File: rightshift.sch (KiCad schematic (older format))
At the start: 15 parts

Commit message: Some minor edits
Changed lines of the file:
@@
 	5825 2425 6125 2425
 Wire Wire Line
-	6125 3625 6125 2425
+	6125 2425 6125 3625
 Wire Wire Line
 	6125 3000 5825 3000
@@
 	4775 3575 4775 3625
 Wire Wire Line
-	4750 3625 6125 3625
+	6125 3625 4750 3625
 Wire Wire Line
 	5825 3625 5825 3575

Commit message: Fix all key annotations
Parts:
- renumbered RS1 to K_RS1, RS2 to K_RS2, RS3 to K_RS3, RS4 to K_RS4, RS5 to K_RS5, RS6 to K_RS6, RS7 to K_RS7, RS8 to K_RS8, RS9 to K_RS9
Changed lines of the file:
@@
 $EndDescr
 $Comp
-L MX-1U RS1
+L MX-1U K_RS1
 U 1 1 591D166F
 P 4800 2250
-F 0 "RS1" H 4800 2375 60  0000 C CNN
+F 0 "K_RS1" H 4800 2375 60  0000 C CNN
 F 1 "MX-1U" H 4800 2300 20  0000 C CNN
 F 2 "" H 4775 2225 60  0001 C CNN
@@
 $EndComp
 $Comp
-L MX-1.25U RS2
+L MX-1.25U K_RS2
 U 1 1 591D16FE
 P 4800 2825
-F 0 "RS2" H 4800 2950 60  0000 C CNN
+F 0 "K_RS2" H 4800 2950 60  0000 C CNN
 F 1 "MX-1.25U" H 4800 2875 20  0000 C CNN
 F 2 "" H 4775 2800 60  0001 C CNN
@@
 $EndComp
 $Comp
-L MX-1.25U RS3
+L MX-1.25U K_RS3
 U 1 1 591D173D
 P 4800 3400
-F 0 "RS3" H 4800 3525 60  0000 C CNN
+F 0 "K_RS3" H 4800 3525 60  0000 C CNN
 F 1 "MX-1.25U" H 4800 3450 20  0000 C CNN
 F 2 "" H 4775 3375 60  0001 C CNN
@@
 $EndComp
 $Comp
-L MX-1U RS4
+L MX-1U K_RS4
 U 1 1 591D189D
 P 5325 2250
-F 0 "RS4" H 5325 2375 60  0000 C CNN
+F 0 "K_RS4" H 5325 2375 60  0000 C CNN
 F 1 "MX-1U" H 5325 2300 20  0000 C CNN
 F 2 "" H 5300 2225 60  0001 C CNN
@@
 $EndComp
 $Comp
-L MX-1.75U RS5
+L MX-1.75U K_RS5
 U 1 1 591D19CC
 P 5325 2825
-F 0 "RS5" H 5325 2950 60  0000 C CNN
+F 0 "K_RS5" H 5325 2950 60  0000 C CNN
 F 1 "MX-1.75U" H 5325 2875 20  0000 C CNN
 F 2 "" H 5300 2800 60  0001 C CNN
@@
 $EndComp
 $Comp
-L MX-2.75U RS6
+L MX-2.75U K_RS6
 U 1 1 591D1A90
 P 5325 3400
-F 0 "RS6" H 5325 3525 60  0000 C CNN
+F 0 "K_RS6" H 5325 3525 60  0000 C CNN
 F 1 "MX-2.75U" H 5325 3450 20  0000 C CNN
 F 2 "" H 5300 3375 60  0001 C CNN
@@
 $EndComp
 $Comp
-L MX-1U RS7
+L MX-1U K_RS7
 U 1 1 591D21A1
 P 5850 2250
-F 0 "RS7" H 5850 2375 60  0000 C CNN
+F 0 "K_RS7" H 5850 2375 60  0000 C CNN
 F 1 "MX-1U" H 5850 2300 20  0000 C CNN
 F 2 "" H 5825 2225 60  0001 C CNN
@@
 $EndComp
 $Comp
-L MX-1.75U RS8
+L MX-1.75U K_RS8
 U 1 1 591D25C2
 P 5850 2825
-F 0 "RS8" H 5850 2950 60  0000 C CNN
+F 0 "K_RS8" H 5850 2950 60  0000 C CNN
 F 1 "MX-1.75U" H 5850 2875 20  0000 C CNN
 F 2 "" H 5825 2800 60  0001 C CNN
@@
 $EndComp
 $Comp
-L MX-2U RS9
+L MX-2U K_RS9
 U 1 1 591D28C1
 P 5850 3400
-F 0 "RS9" H 5850 3525 60  0000 C CNN
+F 0 "K_RS9" H 5850 3525 60  0000 C CNN
 F 1 "MX-2U" H 5850 3450 20  0000 C CNN
 F 2 "" H 5825 3375 60  0001 C CNN

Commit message: Fix left shift, associate MX footprints
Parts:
- K_RS1, K_RS4, K_RS7: footprint (none) -> MX_Alps_Hybrid:MX-1U
- K_RS2, K_RS3: footprint (none) -> MX_Alps_Hybrid:MX-1.25U
- K_RS5, K_RS8: footprint (none) -> MX_Alps_Hybrid:MX-1.75U
- K_RS6: footprint (none) -> MX_Alps_Hybrid:MX-2.75U
- K_RS9: footprint (none) -> MX_Alps_Hybrid:MX-2U
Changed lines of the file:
@@
 F 0 "K_RS1" H 4800 2375 60  0000 C CNN
 F 1 "MX-1U" H 4800 2300 20  0000 C CNN
-F 2 "" H 4775 2225 60  0001 C CNN
+F 2 "MX_Alps_Hybrid:MX-1U" H 4775 2225 60  0001 C CNN
 F 3 "" H 4775 2225 60  0001 C CNN
 	1    4800 2250
@@
 F 0 "K_RS2" H 4800 2950 60  0000 C CNN
 F 1 "MX-1.25U" H 4800 2875 20  0000 C CNN
-F 2 "" H 4775 2800 60  0001 C CNN
+F 2 "MX_Alps_Hybrid:MX-1.25U" H 4775 2800 60  0001 C CNN
 F 3 "" H 4775 2800 60  0001 C CNN
 	1    4800 2825
@@
 F 0 "K_RS3" H 4800 3525 60  0000 C CNN
 F 1 "MX-1.25U" H 4800 3450 20  0000 C CNN
-F 2 "" H 4775 3375 60  0001 C CNN
+F 2 "MX_Alps_Hybrid:MX-1.25U" H 4775 3375 60  0001 C CNN
 F 3 "" H 4775 3375 60  0001 C CNN
 	1    4800 3400
@@
 F 0 "K_RS4" H 5325 2375 60  0000 C CNN
 F 1 "MX-1U" H 5325 2300 20  0000 C CNN
-F 2 "" H 5300 2225 60  0001 C CNN
+F 2 "MX_Alps_Hybrid:MX-1U" H 5300 2225 60  0001 C CNN
 F 3 "" H 5300 2225 60  0001 C CNN
 	1    5325 2250
@@
 F 0 "K_RS5" H 5325 2950 60  0000 C CNN
 F 1 "MX-1.75U" H 5325 2875 20  0000 C CNN
-F 2 "" H 5300 2800 60  0001 C CNN
+F 2 "MX_Alps_Hybrid:MX-1.75U" H 5300 2800 60  0001 C CNN
 F 3 "" H 5300 2800 60  0001 C CNN
 	1    5325 2825
@@
 F 0 "K_RS6" H 5325 3525 60  0000 C CNN
 F 1 "MX-2.75U" H 5325 3450 20  0000 C CNN
-F 2 "" H 5300 3375 60  0001 C CNN
+F 2 "MX_Alps_Hybrid:MX-2.75U" H 5300 3375 60  0001 C CNN
 F 3 "" H 5300 3375 60  0001 C CNN
 	1    5325 3400
@@
 F 0 "K_RS7" H 5850 2375 60  0000 C CNN
 F 1 "MX-1U" H 5850 2300 20  0000 C CNN
-F 2 "" H 5825 2225 60  0001 C CNN
+F 2 "MX_Alps_Hybrid:MX-1U" H 5825 2225 60  0001 C CNN
 F 3 "" H 5825 2225 60  0001 C CNN
 	1    5850 2250
@@
 F 0 "K_RS8" H 5850 2950 60  0000 C CNN
 F 1 "MX-1.75U" H 5850 2875 20  0000 C CNN
-F 2 "" H 5825 2800 60  0001 C CNN
+F 2 "MX_Alps_Hybrid:MX-1.75U" H 5825 2800 60  0001 C CNN
 F 3 "" H 5825 2800 60  0001 C CNN
 	1    5850 2825
@@
 F 0 "K_RS9" H 5850 3525 60  0000 C CNN
 F 1 "MX-2U" H 5850 3450 20  0000 C CNN
-F 2 "" H 5825 3375 60  0001 C CNN
+F 2 "MX_Alps_Hybrid:MX-2U" H 5825 3375 60  0001 C CNN
 F 3 "" H 5825 3375 60  0001 C CNN
 	1    5850 3400
@@
 F 0 "DRS1" H 5050 1950 50  0000 C CNN
 F 1 "1N4148WS" H 5050 1750 50  0000 C CNN
-F 2 "" H 5050 1850 50  0000 C CNN
+F 2 "" H 5050 1850 50  0001 C CNN
 F 3 "" H 5050 1850 50  0000 C CNN
 	1    5050 1850
@@
 F 0 "DRS2" H 5575 1950 50  0000 C CNN
 F 1 "1N4148WS" H 5575 1750 50  0000 C CNN
-F 2 "" H 5575 1850 50  0000 C CNN
+F 2 "" H 5575 1850 50  0001 C CNN
 F 3 "" H 5575 1850 50  0000 C CNN
 	1    5575 1850
@@
 F 0 "DRS3" H 6100 1950 50  0000 C CNN
 F 1 "1N4148WS" H 6100 1750 50  0000 C CNN
-F 2 "" H 6100 1850 50  0000 C CNN
+F 2 "" H 6100 1850 50  0001 C CNN
 F 3 "" H 6100 1850 50  0000 C CNN
 	1    6100 1850
@@
 F 0 "RRS1" V 5180 3950 50  0000 C CNN
 F 1 "2.2k" V 5100 3950 50  0000 C CNN
-F 2 "" V 5030 3950 50  0000 C CNN
+F 2 "" V 5030 3950 50  0001 C CNN
 F 3 "" H 5100 3950 50  0000 C CNN
 	1    5100 3950
@@
 F 0 "RRS2" V 5705 3950 50  0000 C CNN
 F 1 "2.2k" V 5625 3950 50  0000 C CNN
-F 2 "" V 5555 3950 50  0000 C CNN
+F 2 "" V 5555 3950 50  0001 C CNN
 F 3 "" H 5625 3950 50  0000 C CNN
 	1    5625 3950
@@
 F 0 "RRS3" V 6230 3950 50  0000 C CNN
 F 1 "2.2k" V 6150 3950 50  0000 C CNN
-F 2 "" V 6080 3950 50  0000 C CNN
+F 2 "" V 6080 3950 50  0001 C CNN
 F 3 "" H 6150 3950 50  0000 C CNN
 	1    6150 3950

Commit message: Halfway fix RS2
Failed to load cvpcb
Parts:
- K_RS2: value MX-1.25U -> MX-1.75U; footprint MX_Alps_Hybrid:MX-1.25U -> MX_Alps_Hybrid:MX-1.75U
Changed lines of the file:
@@
 P 4800 2825
 F 0 "K_RS2" H 4800 2950 60  0000 C CNN
-F 1 "MX-1.25U" H 4800 2875 20  0000 C CNN
-F 2 "MX_Alps_Hybrid:MX-1.25U" H 4775 2800 60  0001 C CNN
+F 1 "MX-1.75U" H 4800 2875 20  0000 C CNN
+F 2 "MX_Alps_Hybrid:MX-1.75U" H 4775 2800 60  0001 C CNN
 F 3 "" H 4775 2800 60  0001 C CNN
 	1    4800 2825

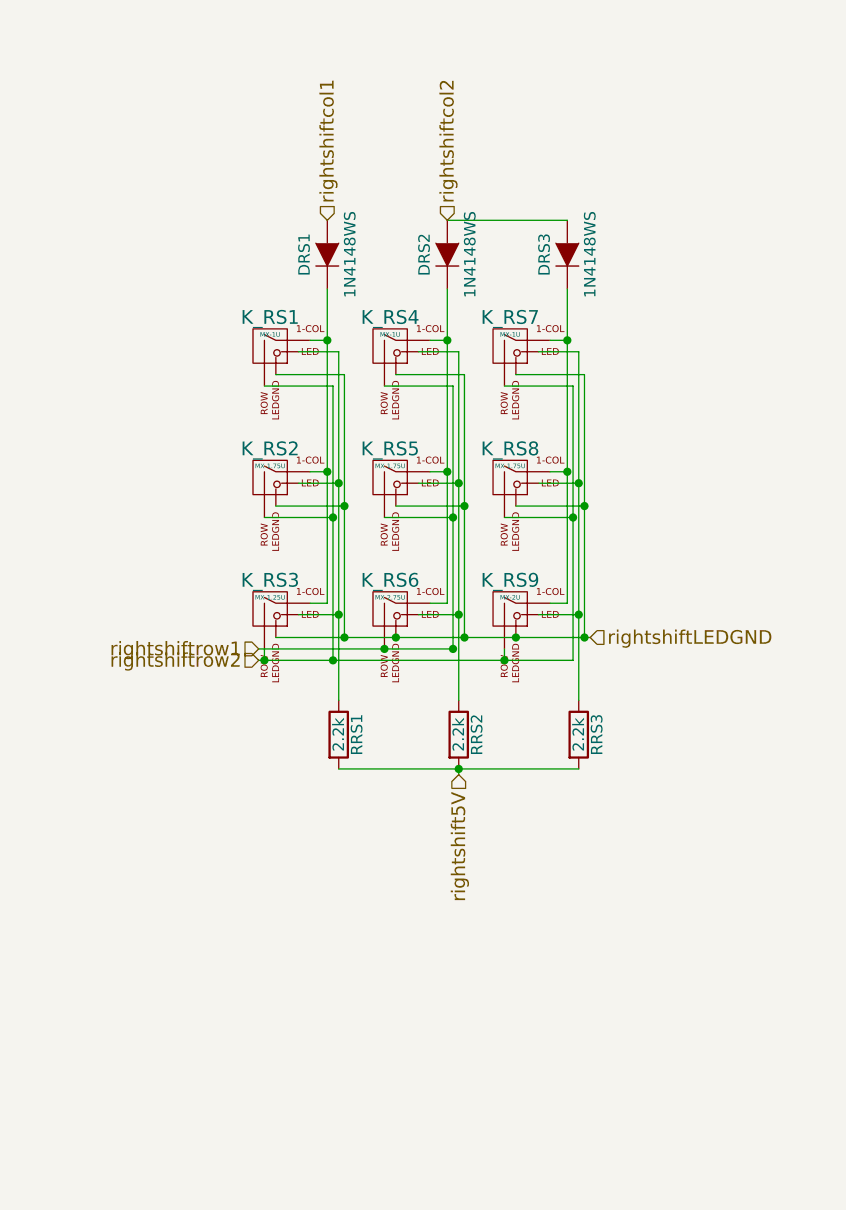
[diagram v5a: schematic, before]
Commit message: Fix RShift Diode Location
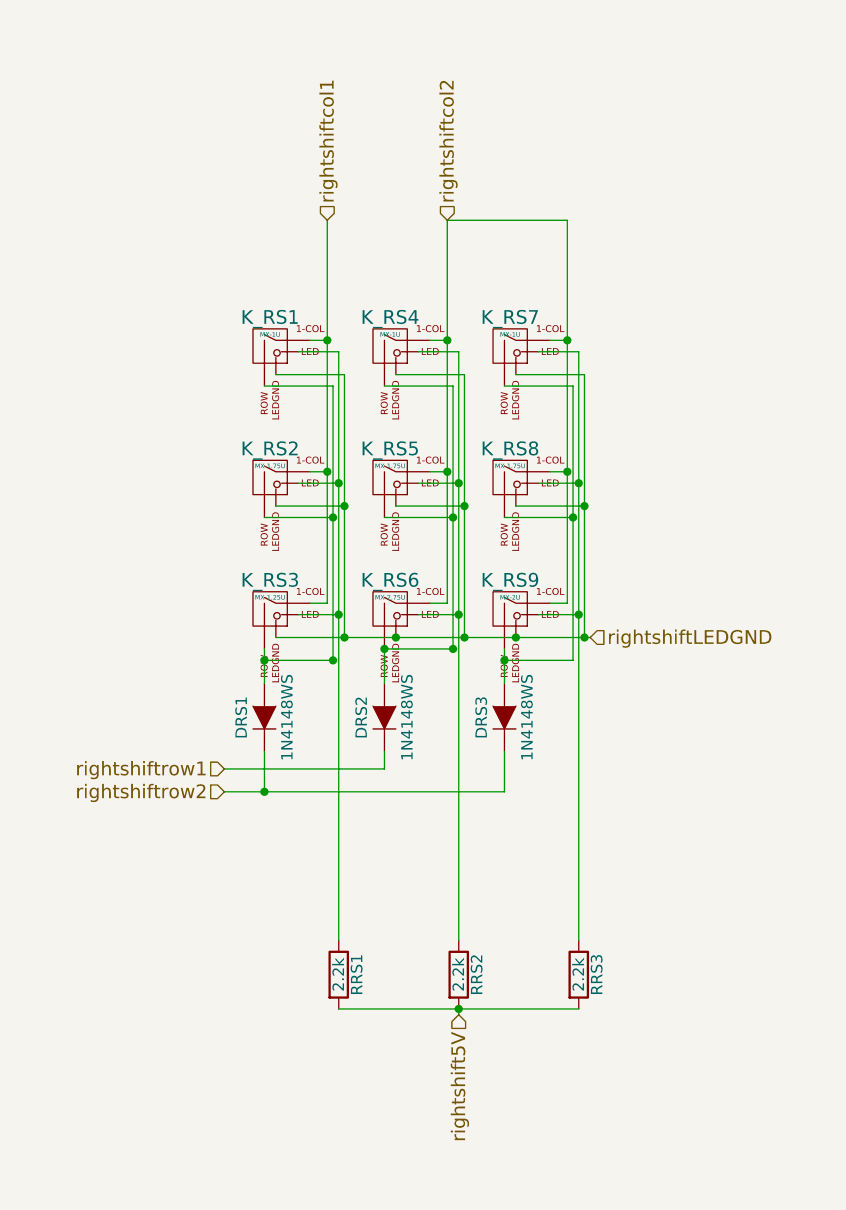
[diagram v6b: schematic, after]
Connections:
- net rightshiftcol1: now also K_RS1.1 (COL), K_RS2.1 (COL), K_RS3.1 (COL); no longer DRS1.2 (A)
- net rightshiftcol2: now also K_RS4.1 (COL), K_RS5.1 (COL), K_RS6.1 (COL), K_RS7.1 (COL), K_RS8.1 (COL), K_RS9.1 (COL); no longer DRS2.2 (A), DRS3.2 (A)
- net rightshiftrow1: now also DRS2.1 (K); no longer K_RS4.2 (ROW), K_RS5.2 (ROW), K_RS6.2 (ROW)
- net rightshiftrow2: now also DRS1.1 (K), DRS3.1 (K); no longer K_RS1.2 (ROW), K_RS2.2 (ROW), K_RS3.2 (ROW), K_RS7.2 (ROW), K_RS8.2 (ROW), K_RS9.2 (ROW)
- new net: DRS1.2 (A), K_RS1.2 (ROW), K_RS2.2 (ROW), K_RS3.2 (ROW)
- new net: DRS2.2 (A), K_RS4.2 (ROW), K_RS5.2 (ROW), K_RS6.2 (ROW)
- new net: DRS3.2 (A), K_RS7.2 (ROW), K_RS8.2 (ROW), K_RS9.2 (ROW)
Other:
- moved on the sheet: DRS1, DRS2, DRS3, RRS1, RRS2, RRS3
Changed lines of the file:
@@
 	4975 2225 5050 2225
 Wire Wire Line
-	5050 2000 5050 3375
+	5050 1700 5050 3375
 Wire Wire Line
 	5050 2800 4975 2800
@@
 	5500 2225 5575 2225
 Wire Wire Line
-	5575 2000 5575 3375
+	5575 1700 5575 3375
 Wire Wire Line
 	5575 2800 5500 2800
@@
 	6025 2225 6100 2225
 Wire Wire Line
-	6100 2000 6100 3375
+	6100 1700 6100 3375
 Wire Wire Line
 	6100 2800 6025 2800
@@
 	5075 3000 4775 3000
 Wire Wire Line
-	5600 3575 4750 3575
+	5600 3575 5300 3575
 Connection ~ 5075 3000
 Wire Wire Line
@@
 	4925 2275 5100 2275
 Wire Wire Line
-	5100 2275 5100 3800
+	5100 2275 5100 4850
 Wire Wire Line
 	5100 2850 4925 2850
@@
 	5450 2275 5625 2275
 Wire Wire Line
-	5625 2275 5625 3800
+	5625 2275 5625 4850
 Wire Wire Line
 	5625 2850 5450 2850
@@
 	5975 2275 6150 2275
 Wire Wire Line
-	6150 2275 6150 3800
+	6150 2275 6150 4850
 Wire Wire Line
 	6150 2850 5975 2850
@@
 L D DRS1
 U 1 1 591D56E3
-P 5050 1850
-F 0 "DRS1" H 5050 1950 50  0000 C CNN
-F 1 "1N4148WS" H 5050 1750 50  0000 C CNN
-F 2 "" H 5050 1850 50  0001 C CNN
-F 3 "" H 5050 1850 50  0000 C CNN
-	1    5050 1850
+P 4775 3875
+F 0 "DRS1" H 4775 3975 50  0000 C CNN
+F 1 "1N4148WS" H 4775 3775 50  0000 C CNN
+F 2 "" H 4775 3875 50  0001 C CNN
+F 3 "" H 4775 3875 50  0000 C CNN
+	1    4775 3875
 	0    -1   -1   0
 $EndComp
@@
 L D DRS2
 U 1 1 591D57BD
-P 5575 1850
-F 0 "DRS2" H 5575 1950 50  0000 C CNN
-F 1 "1N4148WS" H 5575 1750 50  0000 C CNN
-F 2 "" H 5575 1850 50  0001 C CNN
-F 3 "" H 5575 1850 50  0000 C CNN
-	1    5575 1850
+P 5300 3875
+F 0 "DRS2" H 5300 3975 50  0000 C CNN
+F 1 "1N4148WS" H 5300 3775 50  0000 C CNN
+F 2 "" H 5300 3875 50  0001 C CNN
+F 3 "" H 5300 3875 50  0000 C CNN
+	1    5300 3875
 	0    -1   -1   0
 $EndComp
@@
 L D DRS3
 U 1 1 591D583A
-P 6100 1850
-F 0 "DRS3" H 6100 1950 50  0000 C CNN
-F 1 "1N4148WS" H 6100 1750 50  0000 C CNN
-F 2 "" H 6100 1850 50  0001 C CNN
-F 3 "" H 6100 1850 50  0000 C CNN
-	1    6100 1850
+P 5825 3875
+F 0 "DRS3" H 5825 3975 50  0000 C CNN
+F 1 "1N4148WS" H 5825 3775 50  0000 C CNN
+F 2 "" H 5825 3875 50  0001 C CNN
+F 3 "" H 5825 3875 50  0000 C CNN
+	1    5825 3875
 	0    -1   -1   0
 $EndComp
@@
 Connection ~ 6100 2225
 Connection ~ 5575 2225
-Text HLabel 4750 3575 0    60   Input ~ 0
+Text HLabel 4600 4100 0    60   Input ~ 0
 rightshiftrow1
 $Comp
 L R RRS1
 U 1 1 591D6B12
-P 5100 3950
-F 0 "RRS1" V 5180 3950 50  0000 C CNN
-F 1 "2.2k" V 5100 3950 50  0000 C CNN
-F 2 "" V 5030 3950 50  0001 C CNN
-F 3 "" H 5100 3950 50  0000 C CNN
-	1    5100 3950
+P 5100 5000
+F 0 "RRS1" V 5180 5000 50  0000 C CNN
+F 1 "2.2k" V 5100 5000 50  0000 C CNN
+F 2 "" V 5030 5000 50  0001 C CNN
+F 3 "" H 5100 5000 50  0000 C CNN
+	1    5100 5000
 	1    0    0    -1
 $EndComp
@@
 L R RRS2
 U 1 1 591D713D
-P 5625 3950
-F 0 "RRS2" V 5705 3950 50  0000 C CNN
-F 1 "2.2k" V 5625 3950 50  0000 C CNN
-F 2 "" V 5555 3950 50  0001 C CNN
-F 3 "" H 5625 3950 50  0000 C CNN
-	1    5625 3950
+P 5625 5000
+F 0 "RRS2" V 5705 5000 50  0000 C CNN
+F 1 "2.2k" V 5625 5000 50  0000 C CNN
+F 2 "" V 5555 5000 50  0001 C CNN
+F 3 "" H 5625 5000 50  0000 C CNN
+	1    5625 5000
 	1    0    0    -1
 $EndComp
@@
 L R RRS3
 U 1 1 591D71A5
-P 6150 3950
-F 0 "RRS3" V 6230 3950 50  0000 C CNN
-F 1 "2.2k" V 6150 3950 50  0000 C CNN
-F 2 "" V 6080 3950 50  0001 C CNN
-F 3 "" H 6150 3950 50  0000 C CNN
-	1    6150 3950
+P 6150 5000
+F 0 "RRS3" V 6230 5000 50  0000 C CNN
+F 1 "2.2k" V 6150 5000 50  0000 C CNN
+F 2 "" V 6080 5000 50  0001 C CNN
+F 3 "" H 6150 5000 50  0000 C CNN
+	1    6150 5000
 	1    0    0    -1
 $EndComp
@@
 Connection ~ 6150 3425
 Wire Wire Line
-	5100 4100 6150 4100
-Connection ~ 5625 4100
-Text HLabel 5625 4125 3    60   Input ~ 0
+	5100 5150 6150 5150
+Connection ~ 5625 5150
+Text HLabel 5625 5175 3    60   Input ~ 0
 rightshift5V
 Wire Wire Line
-	5625 4125 5625 4100
+	5625 5175 5625 5150
 Text HLabel 6200 3525 2    60   Input ~ 0
 rightshiftLEDGND
 Connection ~ 6175 3525
-Text HLabel 4750 3625 0    60   Input ~ 0
+Text HLabel 4600 4200 0    60   Input ~ 0
 rightshiftrow2
 Wire Wire Line
 	5575 1700 6100 1700
 Wire Wire Line
-	4775 3575 4775 3625
-Wire Wire Line
-	6125 3625 4750 3625
-Wire Wire Line
-	5825 3625 5825 3575
+	4775 3575 4775 3725
+Wire Wire Line
+	6125 3625 5825 3625
+Wire Wire Line
+	5075 3625 4775 3625
+Wire Wire Line
+	5825 3575 5825 3725
 Connection ~ 4775 3625
 Connection ~ 5075 3625
 Connection ~ 5825 3625
+Wire Wire Line
+	4600 4100 5300 4100
+Wire Wire Line
+	5300 4100 5300 4025
+Wire Wire Line
+	5300 3575 5300 3725
+Wire Wire Line
+	4775 4025 4775 4200
+Wire Wire Line
+	4600 4200 5825 4200
+Wire Wire Line
+	5825 4200 5825 4025
+Connection ~ 4775 4200
 $EndSCHEMATC

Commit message: Assign the footprints for every resistor and diode
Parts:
- DRS1, DRS2, DRS3: footprint (none) -> Diodes_SMD:D_SOD-323
- RRS1, RRS2, RRS3: footprint (none) -> Resistors_SMD:R_0603
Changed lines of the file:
@@
 F 0 "DRS1" H 4775 3975 50  0000 C CNN
 F 1 "1N4148WS" H 4775 3775 50  0000 C CNN
-F 2 "" H 4775 3875 50  0001 C CNN
+F 2 "Diodes_SMD:D_SOD-323" H 4775 3875 50  0001 C CNN
 F 3 "" H 4775 3875 50  0000 C CNN
 	1    4775 3875
@@
 F 0 "DRS2" H 5300 3975 50  0000 C CNN
 F 1 "1N4148WS" H 5300 3775 50  0000 C CNN
-F 2 "" H 5300 3875 50  0001 C CNN
+F 2 "Diodes_SMD:D_SOD-323" H 5300 3875 50  0001 C CNN
 F 3 "" H 5300 3875 50  0000 C CNN
 	1    5300 3875
@@
 F 0 "DRS3" H 5825 3975 50  0000 C CNN
 F 1 "1N4148WS" H 5825 3775 50  0000 C CNN
-F 2 "" H 5825 3875 50  0001 C CNN
+F 2 "Diodes_SMD:D_SOD-323" H 5825 3875 50  0001 C CNN
 F 3 "" H 5825 3875 50  0000 C CNN
 	1    5825 3875
@@
 F 0 "RRS1" V 5180 5000 50  0000 C CNN
 F 1 "2.2k" V 5100 5000 50  0000 C CNN
-F 2 "" V 5030 5000 50  0001 C CNN
+F 2 "Resistors_SMD:R_0603" V 5030 5000 50  0001 C CNN
 F 3 "" H 5100 5000 50  0000 C CNN
 	1    5100 5000
@@
 F 0 "RRS2" V 5705 5000 50  0000 C CNN
 F 1 "2.2k" V 5625 5000 50  0000 C CNN
-F 2 "" V 5555 5000 50  0001 C CNN
+F 2 "Resistors_SMD:R_0603" V 5555 5000 50  0001 C CNN
 F 3 "" H 5625 5000 50  0000 C CNN
 	1    5625 5000
@@
 F 0 "RRS3" V 6230 5000 50  0000 C CNN
 F 1 "2.2k" V 6150 5000 50  0000 C CNN
-F 2 "" V 6080 5000 50  0001 C CNN
+F 2 "Resistors_SMD:R_0603" V 6080 5000 50  0001 C CNN
 F 3 "" H 6150 5000 50  0000 C CNN
 	1    6150 5000
